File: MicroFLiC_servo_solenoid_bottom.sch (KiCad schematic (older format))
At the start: 14 parts, among them P1 Header_1x14, P10 Socket_1x4, P2 Socket_1x14, P3 12-way Micro-MaTch, P4 Jack_3.5mm_3pin, P5 Jack_3.5mm_3pin, P6 RCA_3, P7 RCA_3, P8 Socket_1x6, P9 Header_1x4

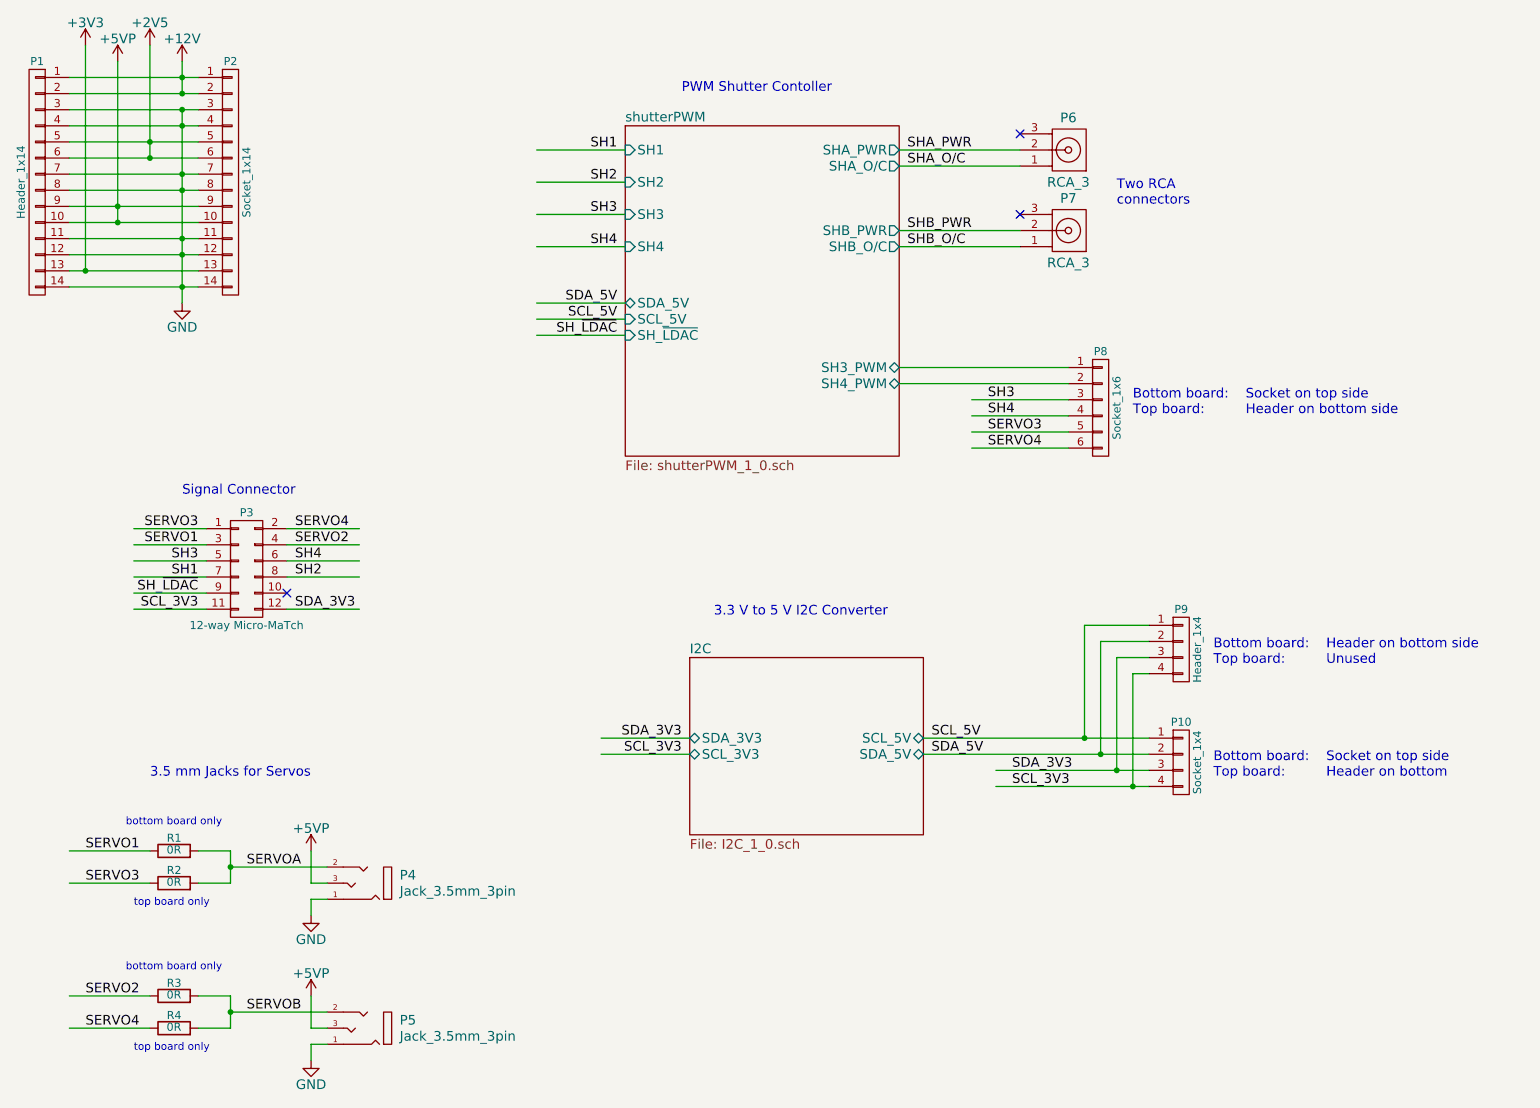
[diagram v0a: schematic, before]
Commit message: Renamed solenoid to v1.1, added part descriptions
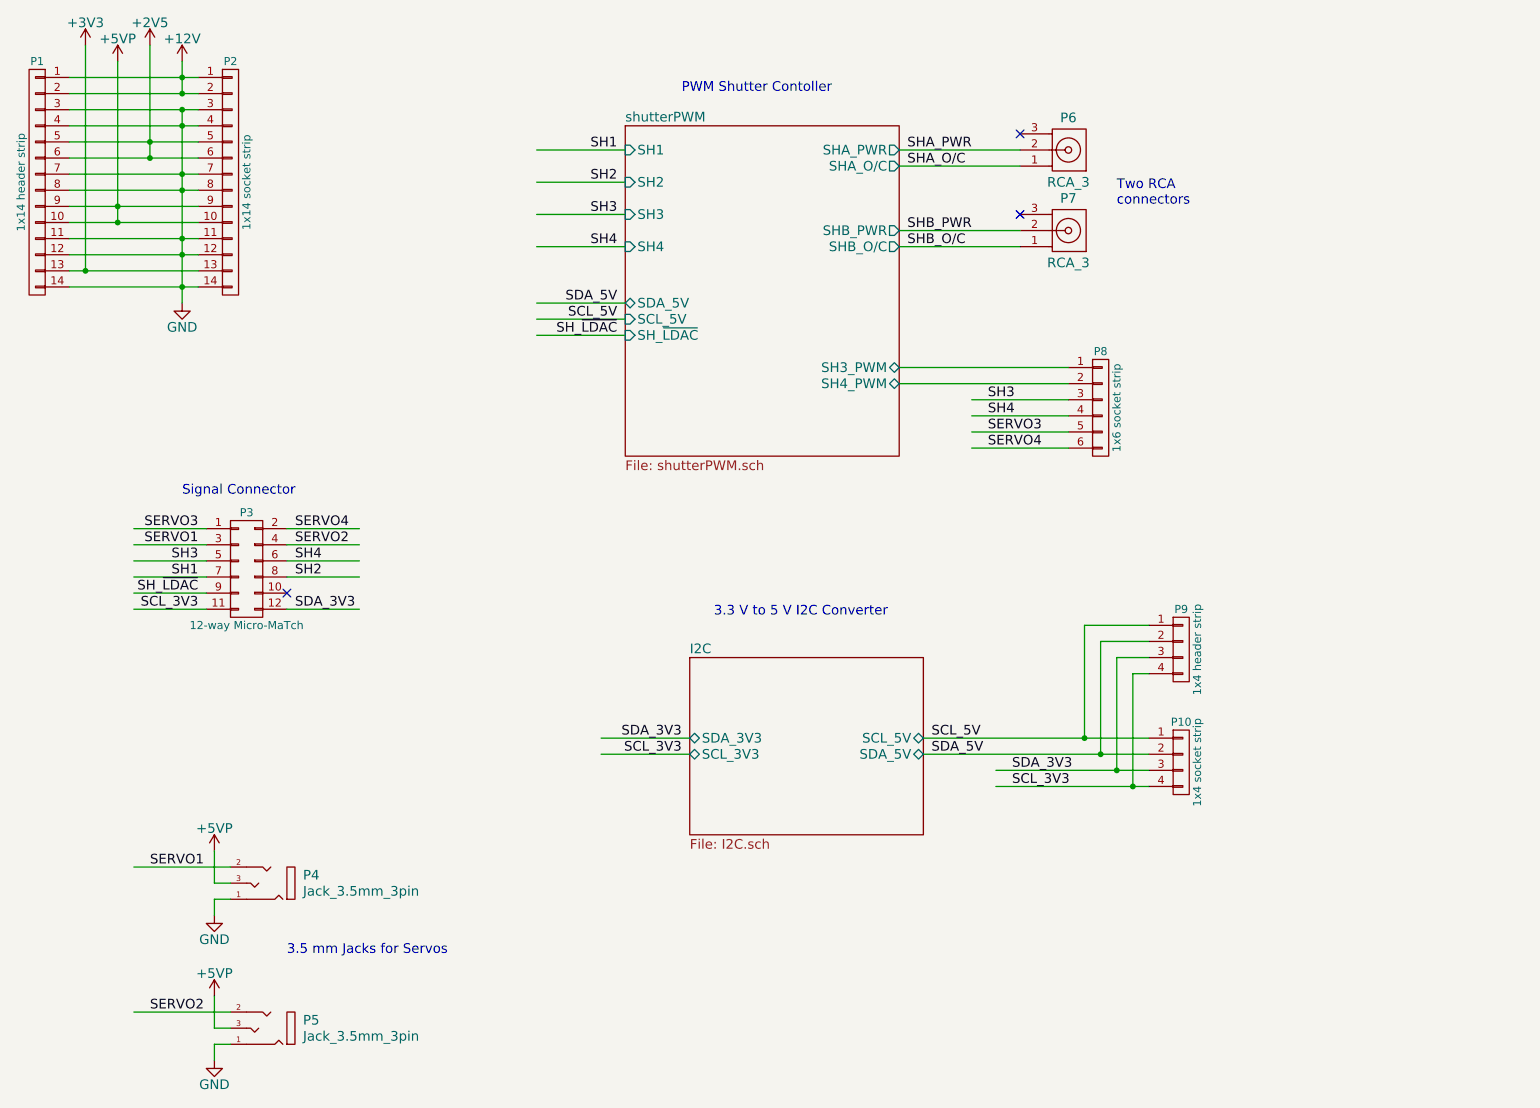
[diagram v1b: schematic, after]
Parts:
- removed R1, R2, R3, R4: 0R, Resistors_SMD:R_0805, symbol R
- P1: value Header_1x14 -> 1x14 header strip; Alt. Order Code (none) -> 855-M20-9991446; Alt. Supplier (none) -> Mouser; Note (none) -> 1x14 header strip; Package (none) -> SIL-14; Supplier (none) -> Farnell
- P10: value Socket_1x4 -> 1x4 socket strip; Alt. Order Code (none) -> ESQ-104-33-G-S; Alt. Supplier (none) -> Samtec; Note (none) -> 1x4 ESQ series elevated socket strip; Package (none) -> SIL-4; Supplier (none) -> Farnell
- P2: value Socket_1x14 -> 1x14 socket strip; Alt. Order Code (none) -> ESQ-114-33-G-S; Alt. Supplier (none) -> Samtec; Note (none) -> 1x14 ESQ series elevated socket strip; Package (none) -> SIL-14; Supplier (none) -> Farnell
- P3: Alt. Order Code (none) -> 571-8-188275-2; Alt. Supplier (none) -> Mouser; Note (none) -> 12-way SMD Micro-MaTch connector; Package (none) -> Micro-MaTch SMD; Supplier (none) -> Farnell
- P4, P5: Alt. Supplier (none) -> N/A; Note (none) -> Right-angle SMD 3.5mm 3-pin jack; Package (none) -> R/A 3.5mm jack; Supplier (none) -> Farnell
- P6, P7: Alt. Supplier (none) -> N/A; Note (none) -> Right-angle RCA jack; Package (none) -> R/A RCA jack; Supplier (none) -> Farnell
- P8: value Socket_1x6 -> 1x6 socket strip; Alt. Order Code (none) -> ESQ-106-33-G-S; Alt. Supplier (none) -> Samtec; Note (none) -> 1x6 ESQ series elevated socket strip; Package (none) -> SIL-6; Supplier (none) -> Farnell
- P9: value Header_1x4 -> 1x4 header strip; Alt. Order Code (none) -> 855-M20-9990445; Alt. Supplier (none) -> Mouser; Manufacturer Samtec -> Harwin; Note (none) -> 1x4 header strip; Package (none) -> SIL-4; Part Number HTSW-104-15-G-S -> M20-9990445; Supplier (none) -> Farnell
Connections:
- net labels removed: SERVOA, SERVOB
- wire segments 81 -> 71
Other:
- note removed: "Bottom board:\nTop board:"
- note removed: "Header on bottom side\nUnused"
- note removed: "Socket on top side\nHeader on bottom"
- note removed: "Socket on top side\nHeader on bottom side"
- note removed: "bottom board only"
- note removed: "top board only"
- moved on the sheet: P4, P5
